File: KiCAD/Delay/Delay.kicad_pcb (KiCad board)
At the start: 2 copper layers, 50 x 100 mm, 68 parts, among them J1 IN, J2 OUT, J3 Conn_01x03, J4 Conn_01x03, U1 TL072, U2 TL072, U3 PT2399, U4 L7805

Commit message: Delay PCB
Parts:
- moved C4 3.56 mm to (137.8, 91.3)
- moved C12 3.14 mm to (142.8, 87.6)
- moved C11 2.73 mm to (137.8, 84.0)
- moved C10 2.32 mm to (137.8, 80.3)
- moved C9 1.91 mm to (137.8, 76.7)
- moved C16 1.70 mm to (142.8, 106.0)
- moved D1 1.70 mm to (131.8, 94.9)
- moved D2 1.70 mm to (131.8, 92.2)
- moved D3 1.70 mm to (131.8, 89.4)
- moved D4 1.70 mm to (131.8, 86.7)
- moved R10 1.70 mm to (131.8, 97.7)
- moved R11 1.70 mm to (131.8, 100.5)
- moved R12 1.70 mm to (131.8, 73.0)
- moved R13 1.70 mm to (131.8, 75.7)
- moved R14 1.70 mm to (131.8, 78.5)
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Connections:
- R2 pad 1: Net-(C1-Pad1) -> Net-(U1B--)
- R2 pad 2: Net-(U1B--) -> Net-(C1-Pad1)
- R3 pad 1: Net-(U1B--) -> DELAY
- R3 pad 2: DELAY -> Net-(U1B--)
- R8 pad 1: Net-(C2-Pad1) -> Net-(D1-A)
- R8 pad 2: Net-(D1-A) -> Net-(C2-Pad1)
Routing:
- net Net-(U3-LPF1-OUT): track 17.8 -> 0.00 mm
- net Net-(U3-OP2-OUT): track 18.6 -> 2.82 mm
- net D OUT: track 53.6 -> 38.0 mm
- net VDD: track 23.8 -> 9.54 mm, vias 10 -> 6
- net Net-(U3-LPF2-IN): track 16.7 -> 5.05 mm
- net D IN: track 15.5 -> 4.38 mm
- net Net-(C22-Pad2): track 16.9 -> 6.00 mm
- net Net-(U3-LPF1-IN): track 19.2 -> 9.76 mm
- net Net-(U3-OP2-IN): track 9.04 -> 0.00 mm
- net Net-(U2B--): track 26.3 -> 17.6 mm
- net Net-(R15-Pad2): track 70.0 -> 61.7 mm
- net Net-(U3-OP1-OUT): track 9.93 -> 2.81 mm
- net Net-(C2-Pad1): track 45.4 -> 41.5 mm
- net DELAY: track 115.9 -> 112.5 mm, vias 1 -> 3
- net Net-(U3-CC0): track 4.62 -> 6.56 mm
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
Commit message: Delay PCB
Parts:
- moved C19 5.00 mm to (162.2, 97.0), turned to 180 degrees
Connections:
- R18 pad 1: Net-(U3-LPF1-IN) -> Net-(C21-Pad2)
- R18 pad 2: Net-(C21-Pad2) -> Net-(U3-LPF1-IN)
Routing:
- net Net-(U3-LPF1-OUT): track 0.00 -> 17.1 mm
- net D OUT: track 38.0 -> 53.7 mm
- net Net-(U3-OP2-OUT): track 2.82 -> 16.7 mm
- net Net-(C22-Pad2): track 6.00 -> 18.3 mm
- net Net-(U3-LPF2-IN): track 5.05 -> 16.6 mm
- net D IN: track 4.38 -> 13.1 mm
- net Net-(R15-Pad2): track 61.7 -> 69.2 mm
- net Net-(U3-OP1-OUT): track 2.81 -> 9.80 mm
- net Net-(U2B--): track 17.6 -> 24.3 mm
- net Net-(U3-LPF1-IN): track 9.76 -> 14.8 mm
- net VDD: track 9.54 -> 5.40 mm, vias 6 -> 2
- net Net-(U3-OP2-IN): track 0.00 -> 3.73 mm
- net GND: track 8.38 -> 6.48 mm, vias 8 -> 6
- net Net-(U2B-+): track 67.3 -> 68.9 mm, vias 0 -> 1
- net Net-(U2A--): track 18.2 -> 17.6 mm

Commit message: Backup Cleanup
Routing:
- net Net-(U2B-+): track 68.9 -> 64.0 mm, vias 1 -> 2
- net GND: track 6.48 -> 3.90 mm, vias 6 -> 4
- net Net-(U3-OP2-OUT): track 16.7 -> 17.6 mm
- net Net-(R24-Pad1): track 55.1 -> 55.9 mm

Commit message: LFO v1-1
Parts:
- removed Ref**: Val**, HackSynth:PancakeLegend Logo - 10mm
- removed Ref**: Val**, HackSynth:CCHS Logo - 10mm
- moved D1 8.25 mm to (131.8, 86.7)
- moved D4 8.25 mm to (131.8, 94.9)
- moved D2 2.75 mm to (131.8, 89.4)
- moved D3 2.75 mm to (131.8, 92.2)
- moved R9 0.05 mm to (131.8, 83.9)
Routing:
- net Net-(D1-A): track 16.4 -> 13.1 mm
- net Net-(U2B--): track 24.3 -> 23.7 mm

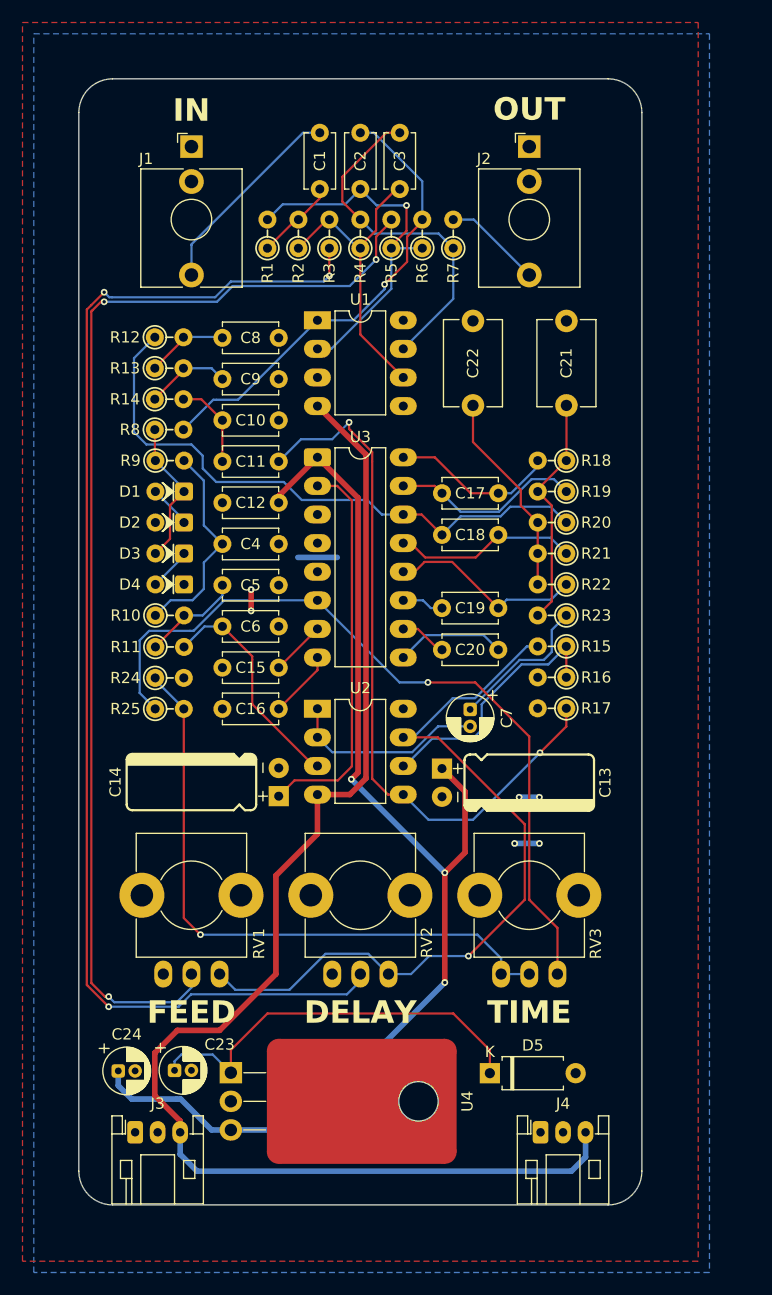
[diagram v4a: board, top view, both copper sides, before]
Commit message: Footprint Edits
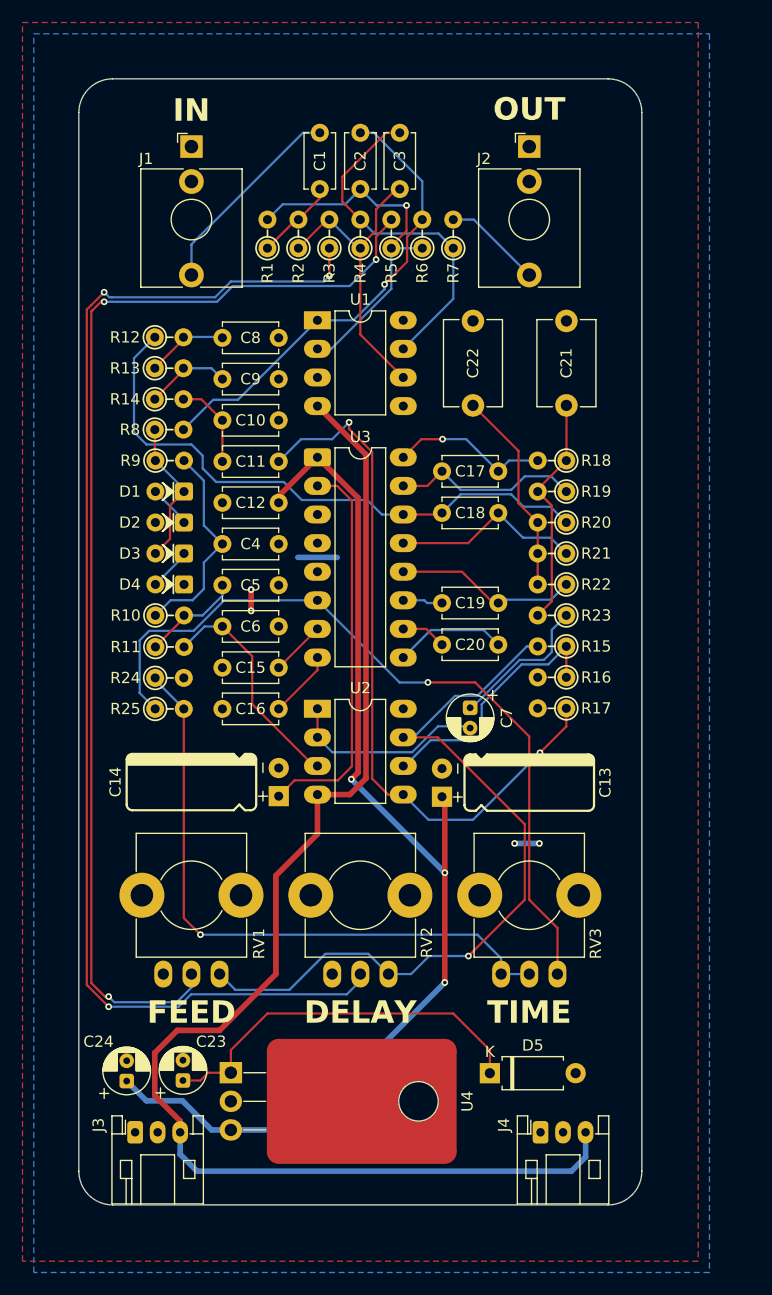
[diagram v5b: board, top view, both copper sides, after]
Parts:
- added Ref**: Val**, HackSynth:Logo - PancakeLegend 10mm, B.Cu at (165.0, 114.0)
- added Ref**: Val**, HackSynth:Logo - CCHS 10mm, B.Cu at (135.0, 114.0)
- C13: footprint HackSynth:CP_Radial_D5.2mm_P2.50mm_LayDown -> HackSynth:CP_Radial_D5.2mm_P2.50mm_LayDown_Mirror
- moved C17 1.95 mm to (162.2, 84.9)
- moved C18 1.95 mm to (157.2, 88.6)
- moved C19 0.45 mm to (162.2, 96.5)
- moved C20 0.45 mm to (157.2, 100.2)
- turned C23 to 90 degrees
- turned C24 to 90 degrees
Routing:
- net +5V: track 105.5 -> 99.6 mm
- net Net-(D5-K): track 36.5 -> 34.3 mm
- net GND: track 3.90 -> 2.41 mm, vias 4 -> 2
- net Net-(U3-LPF2-IN): track 16.6 -> 17.9 mm
- net Net-(U3-OP2-OUT): track 17.4 -> 16.7 mm
- net Net-(U3-LPF1-IN): track 14.8 -> 14.7 mm, vias 0 -> 1
